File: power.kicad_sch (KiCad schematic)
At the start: 58 parts, among them J24 ACT ARMED, J25 PWR IN, J26 ACT DISARMED, J27 ENERGIZE, K1 J115F11C, Q2 NMOS, U36 TLI4971, U37 TLP241A, U38 ADS1110

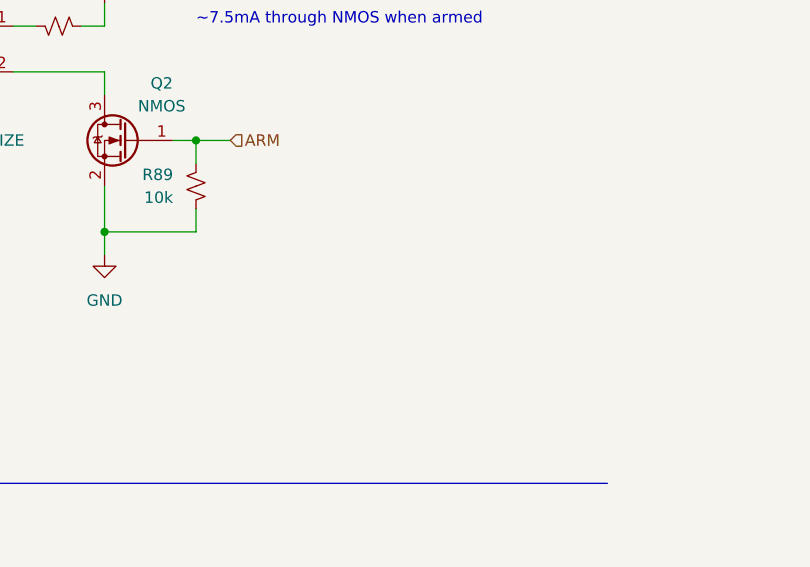
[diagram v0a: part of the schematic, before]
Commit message: LED MPNs and new status indicator
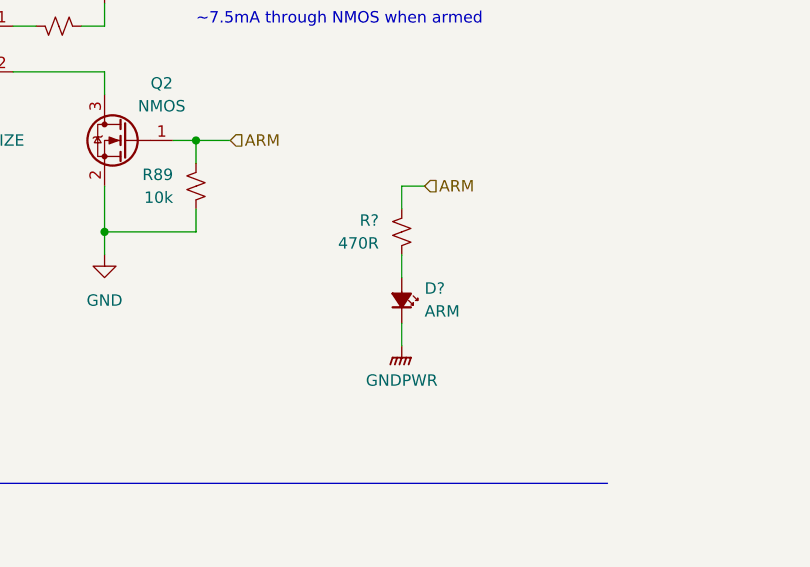
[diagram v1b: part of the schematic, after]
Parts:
- added D?: ARM, LED_SMD:LED_0603_1608Metric, symbol Device:LED_Small_Filled
- added R?: 470R, Resistor_SMD:R_0603_1608Metric, symbol Device:R_Small_US
- D? (x2): MPN (none) -> LTST-C191KGKT
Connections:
- net ARM: now also R?.1
- net GNDPWR: now also D?.1 (K)
- new net: D?.2 (A), R?.2

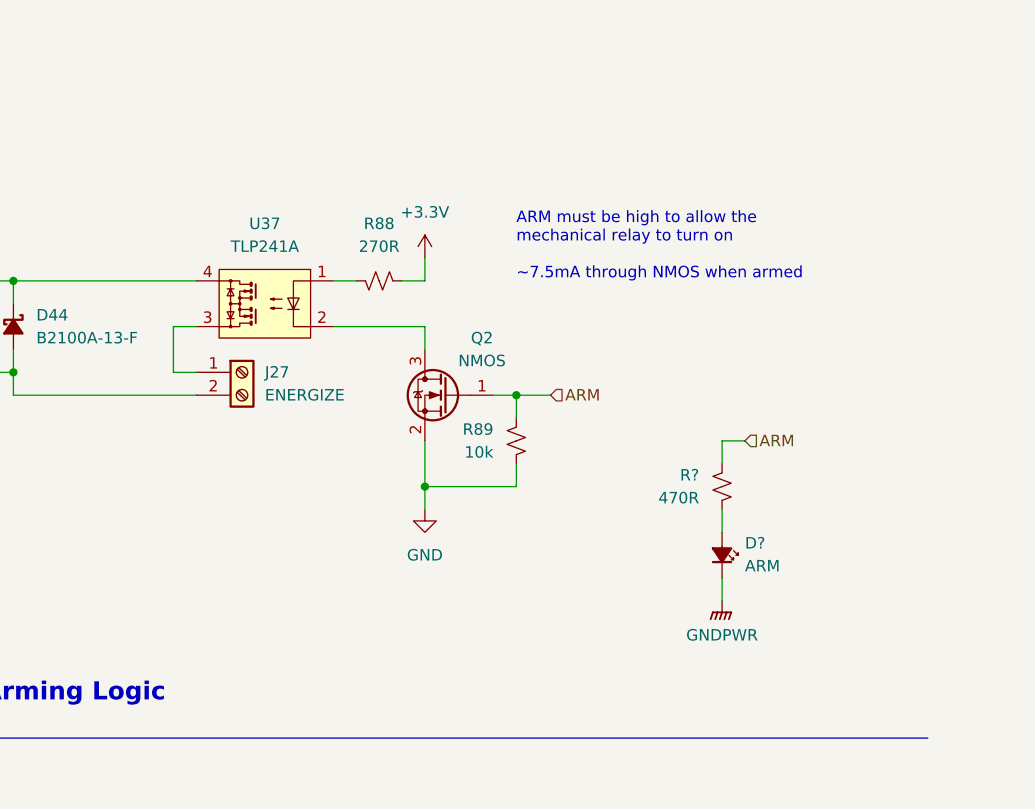
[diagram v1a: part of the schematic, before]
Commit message: Changed status LED configuration
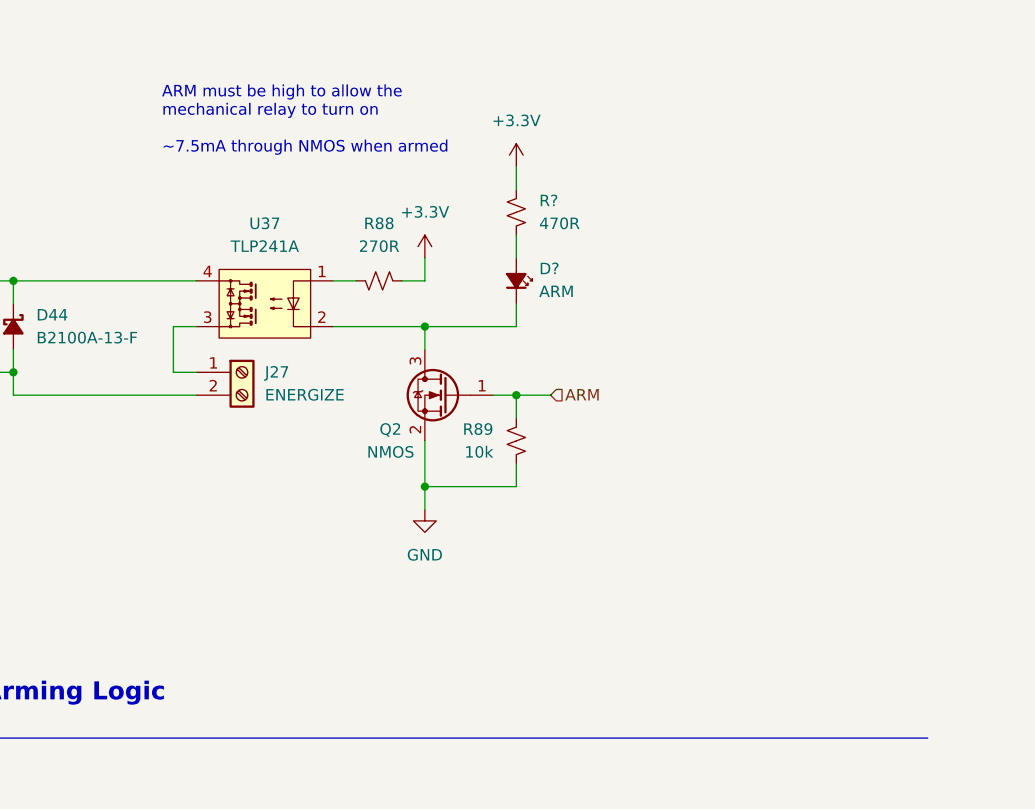
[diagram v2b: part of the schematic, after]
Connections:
- net +3.3V: now also R?.1
- net ARM: no longer R?.1
- net GNDPWR: no longer D?.1 (K)
- net at Q2.3 (D), U37.2: now also D?.1 (K)
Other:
- moved on the sheet: D?, R?

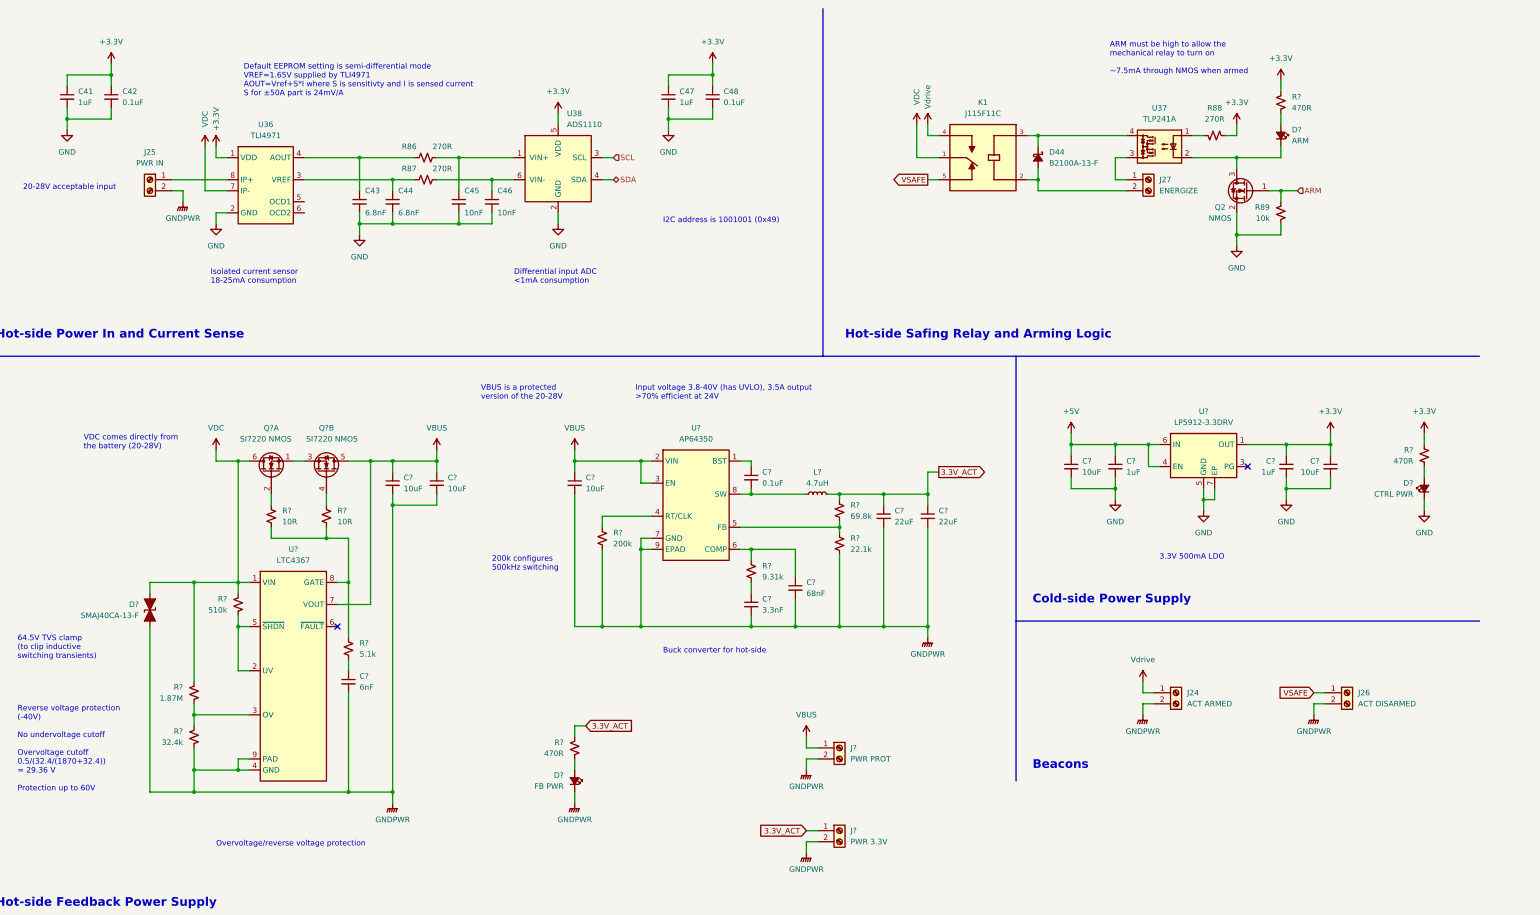
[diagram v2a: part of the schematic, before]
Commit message: Safing jumper, status LEDs, better naming of power states
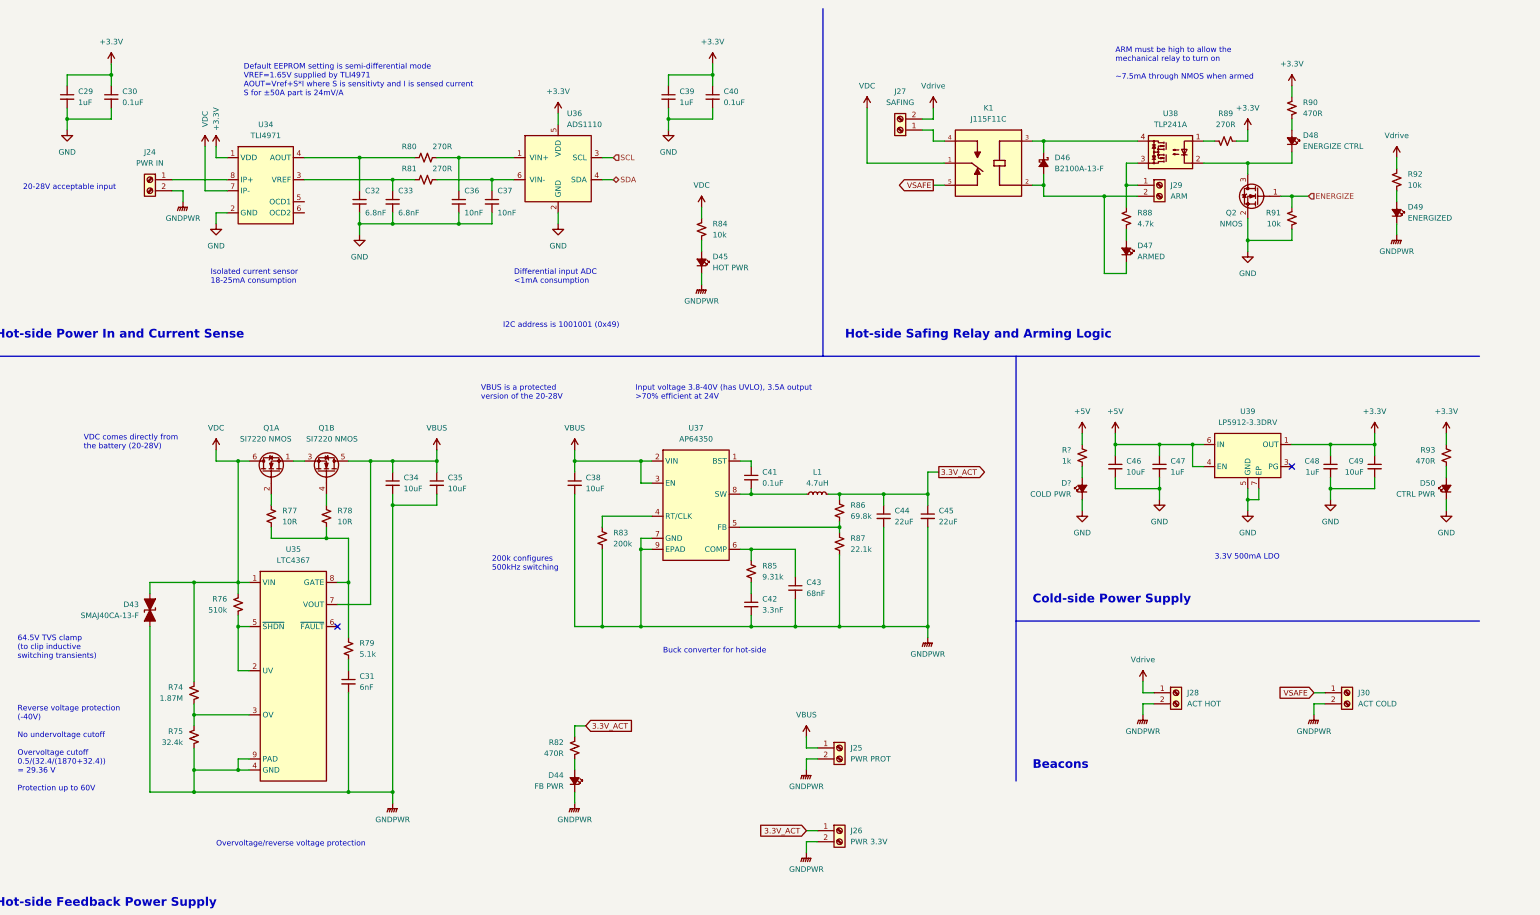
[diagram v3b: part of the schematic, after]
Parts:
- added D45: HOT PWR, LED_SMD:LED_0603_1608Metric, symbol Device:LED_Small_Filled
- added D47: ARMED, LED_SMD:LED_0603_1608Metric, symbol Device:LED_Small_Filled
- added D49: ENERGIZED, LED_SMD:LED_0603_1608Metric, symbol Device:LED_Small_Filled
- added D?: COLD PWR, LED_SMD:LED_0603_1608Metric, symbol Device:LED_Small_Filled
- added J27: SAFING, actuation:1773976, symbol Connector:Screw_Terminal_01x02
- added R84, R92: 10k, Resistor_SMD:R_0603_1608Metric, symbol Device:R_Small_US
- added R88: 4.7k, Resistor_SMD:R_0603_1608Metric, symbol Device:R_Small_US
- added R?: 1k, Resistor_SMD:R_0603_1608Metric, symbol Device:R_Small_US
- D48: renamed from D?; value ARM -> ENERGIZE CTRL; MPN LTST-C191KFKT -> LTST-C191KRKT
- J28: renamed from J24; value ACT ARMED -> ACT HOT
- J29: renamed from J27; value ENERGIZE -> ARM
- J30: renamed from J26; value ACT DISARMED -> ACT COLD
- gave numbers to parts that had none: 36
- renumbered C41 to C29, C42 to C30, C43 to C32, C44 to C33, C45 to C36, C46 to C37, C47 to C39, C48 to C40, D44 to D46, J25 to J24, R86 to R80, R87 to R81, R88 to R89, R89 to R91, U36 to U34, U38 to U36, U37 to U38
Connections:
- net +5V: now also R?.1
- net GND: now also D?.1 (K)
- net GNDPWR: now also D45.1 (K), D49.1 (K)
- net VDC: now also R84.1
- net Vdrive: now also J27.2 (Pin_2), R92.1; no longer K1.4
- net at J29.1 (Pin_1), U38.3: now also R88.1
- net at D46.2 (A), J29.2 (Pin_2), K1.2: now also D47.1 (K)
- net ARM renamed ENERGIZE
- new net: D?.2 (A), R?.2
- new net: J27.1 (Pin_1), K1.4
- new net: D47.2 (A), R88.2
- new net: D45.2 (A), R84.2
- new net: D49.2 (A), R92.2
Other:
- moved on the sheet: C46, C47, C48, C49, D46, D48, D50, J29, K1, Q2, R89, R90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

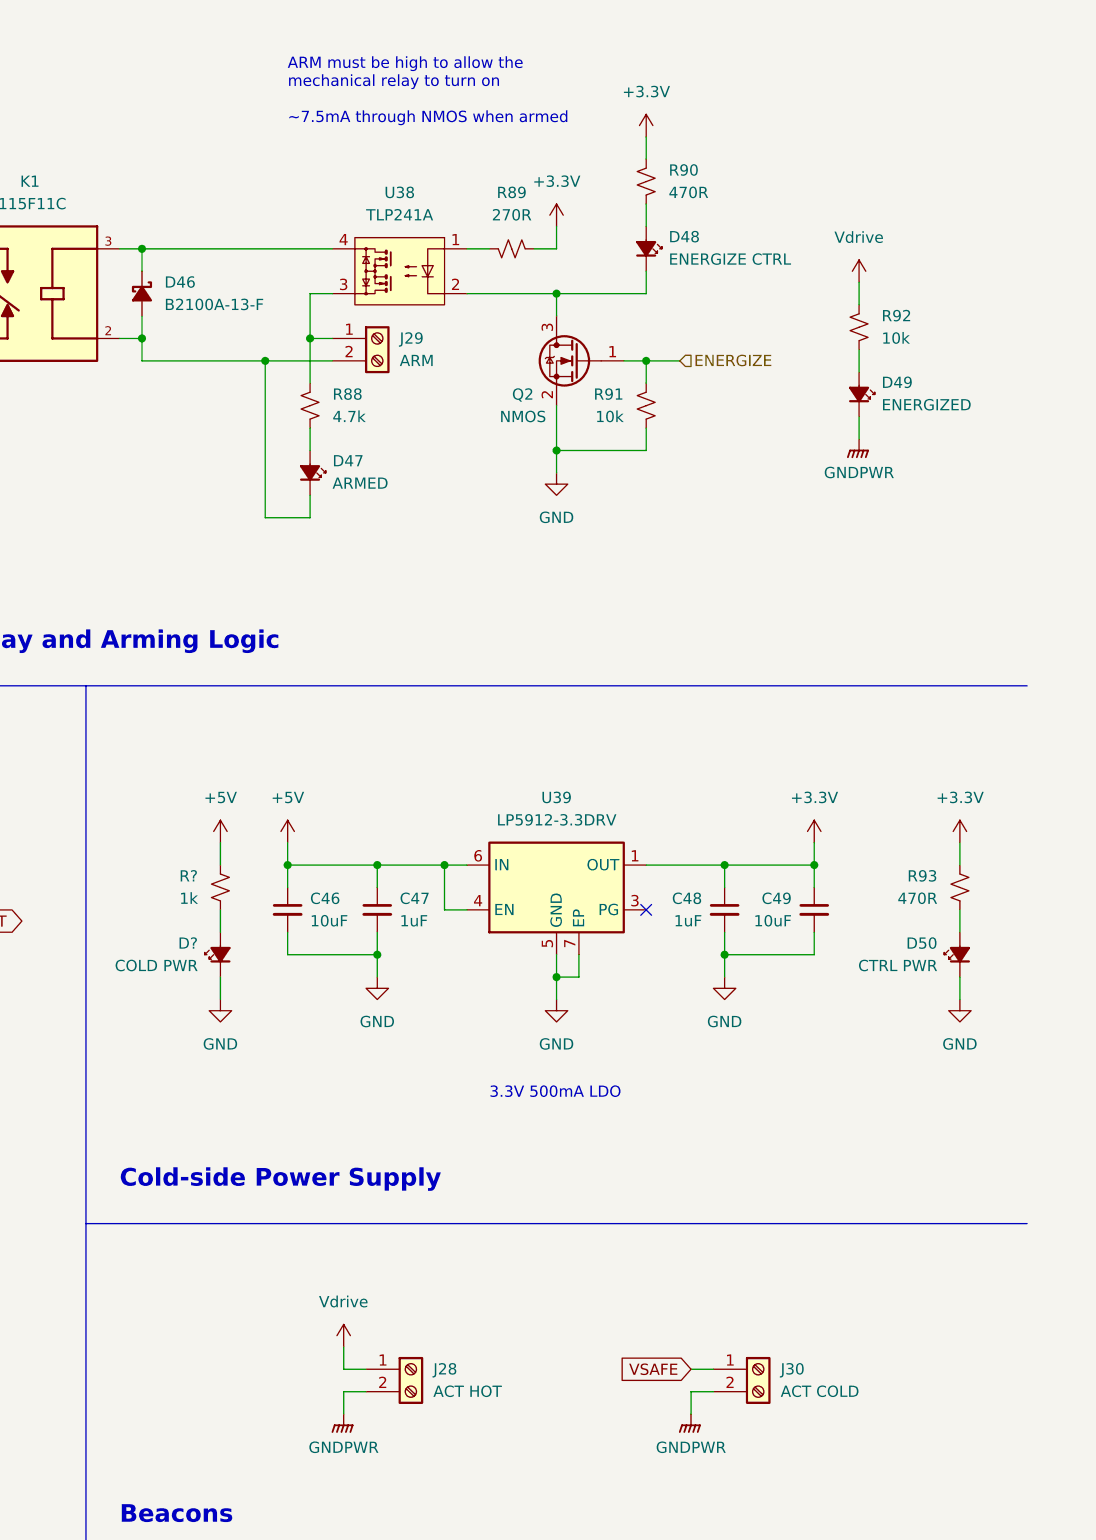
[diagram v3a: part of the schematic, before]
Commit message: Fixing up footprints
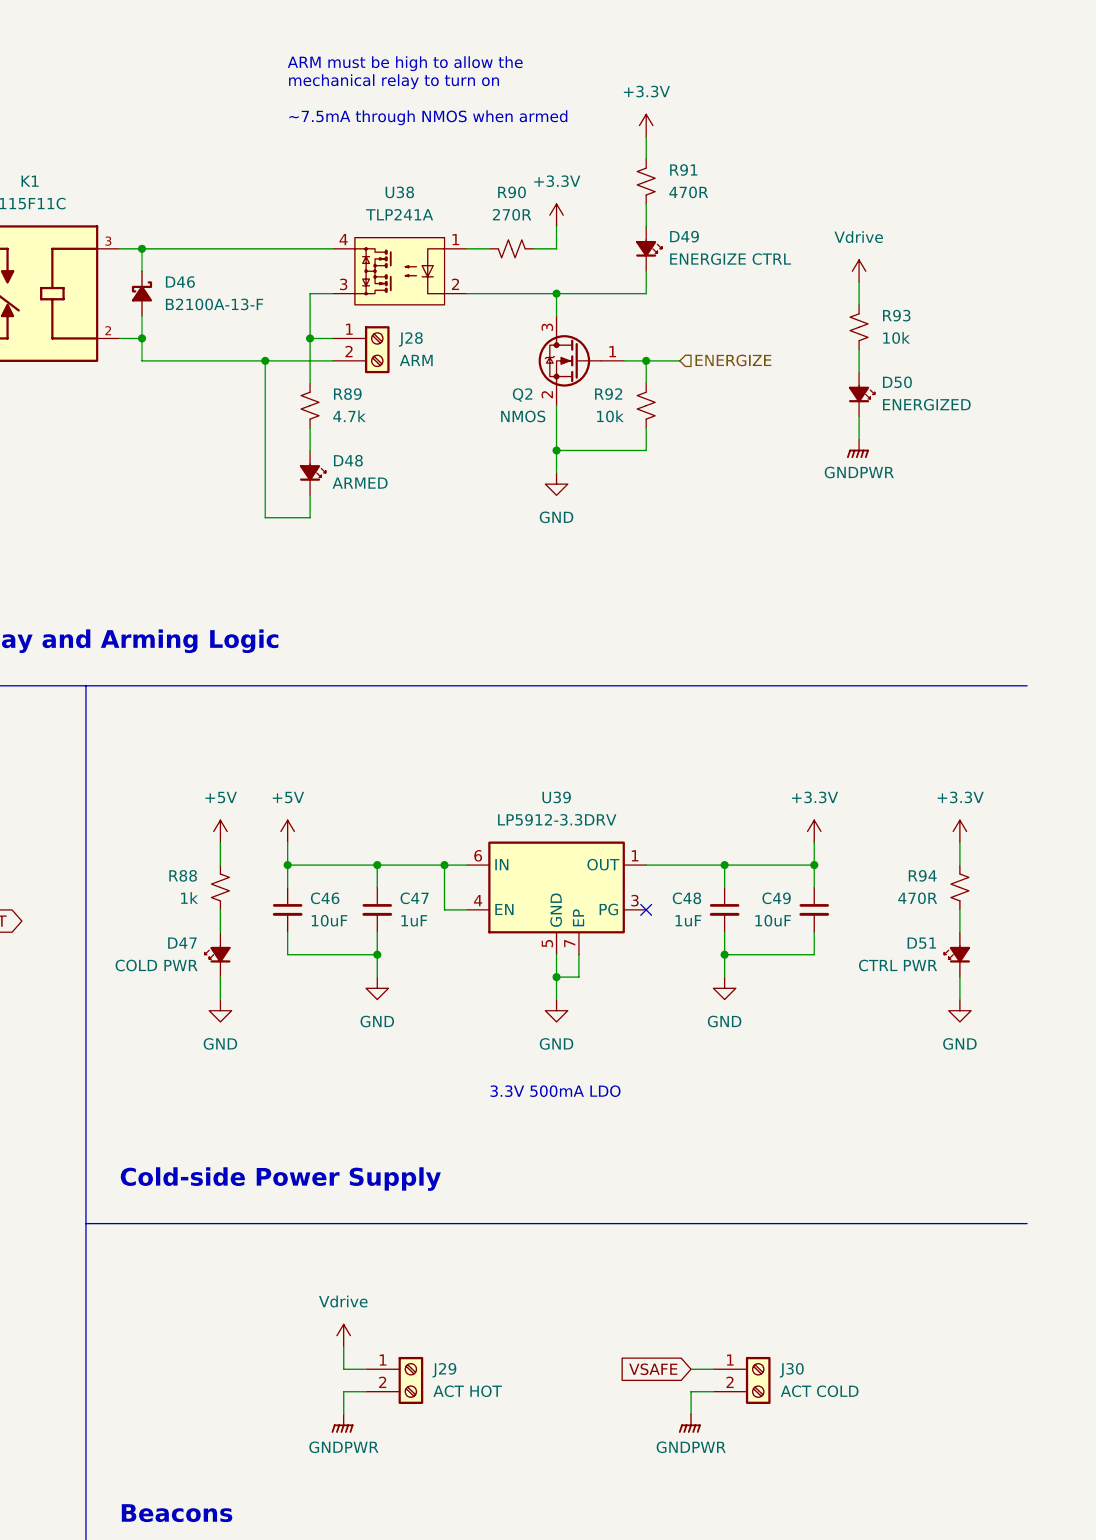
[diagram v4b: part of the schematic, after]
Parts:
- R80, R81: MPN (none) -> RC0603FR-07270RL
- U39: MPN (none) -> LP5912-3.3DRVR
- gave numbers to parts that had none: 2
- renumbered D47 to D48, D48 to D49, D49 to D50, D50 to D51, J29 to J28, J28 to J29, R88 to R89, R89 to R90, R90 to R91, R91 to R92, R92 to R93, R93 to R94

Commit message: MPN reassignment
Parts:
- J25, J26, J28, J29, J30: footprint TerminalBlock_Phoenix:TerminalBlock_Phoenix_PT-1,5-2-5.0-H_1x02_P5.00mm_Horizontal -> actuation:1989447
- U39: footprint Package_SON:WSON-6-1EP_2x2mm_P0.65mm_EP1x1.6mm_ThermalVias -> Package_SON:WSON-6-1EP_2x2mm_P0.65mm_EP1x1.6mm
